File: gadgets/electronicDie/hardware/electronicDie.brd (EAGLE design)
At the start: 43.2 x 69.8 mm, 30 parts, among them IC1 CD4029N, IC2 NE555N, T1 BC327, T2 BC337, X1 USBPCB

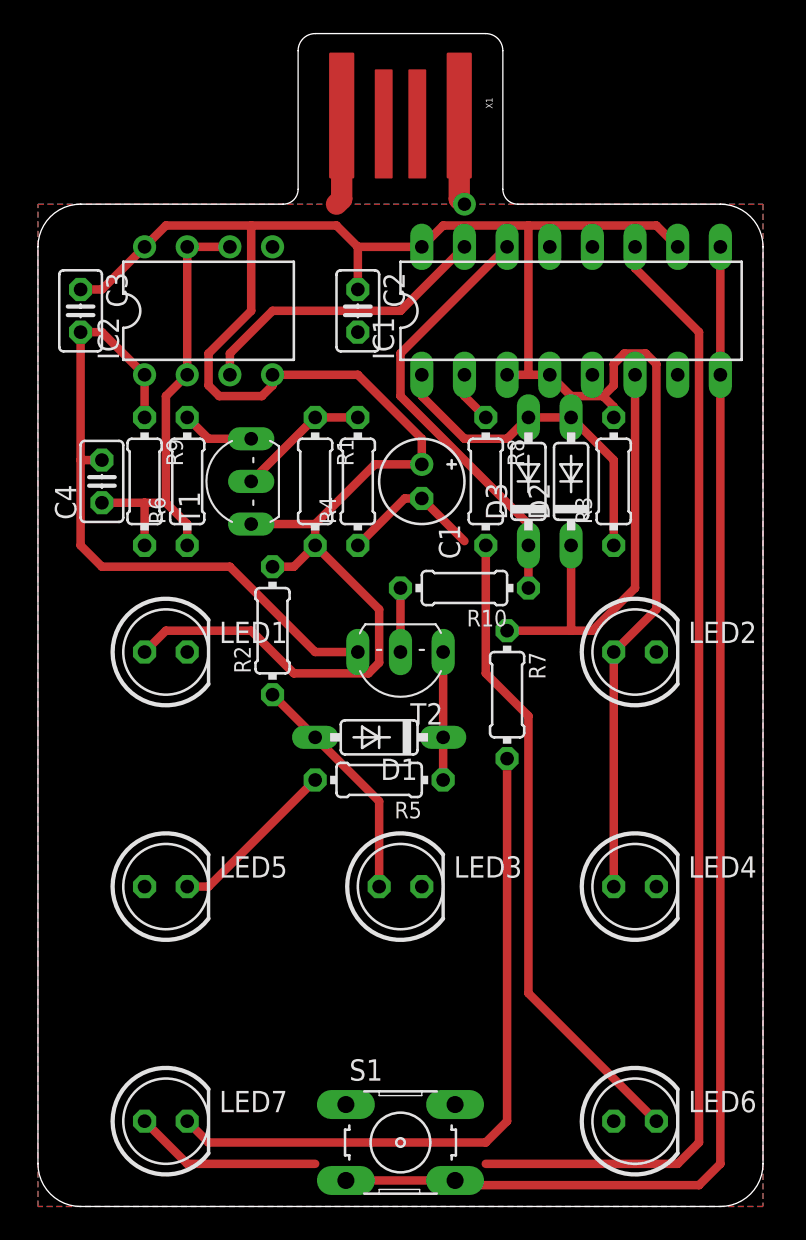
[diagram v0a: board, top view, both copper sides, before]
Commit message: Add silkscreen
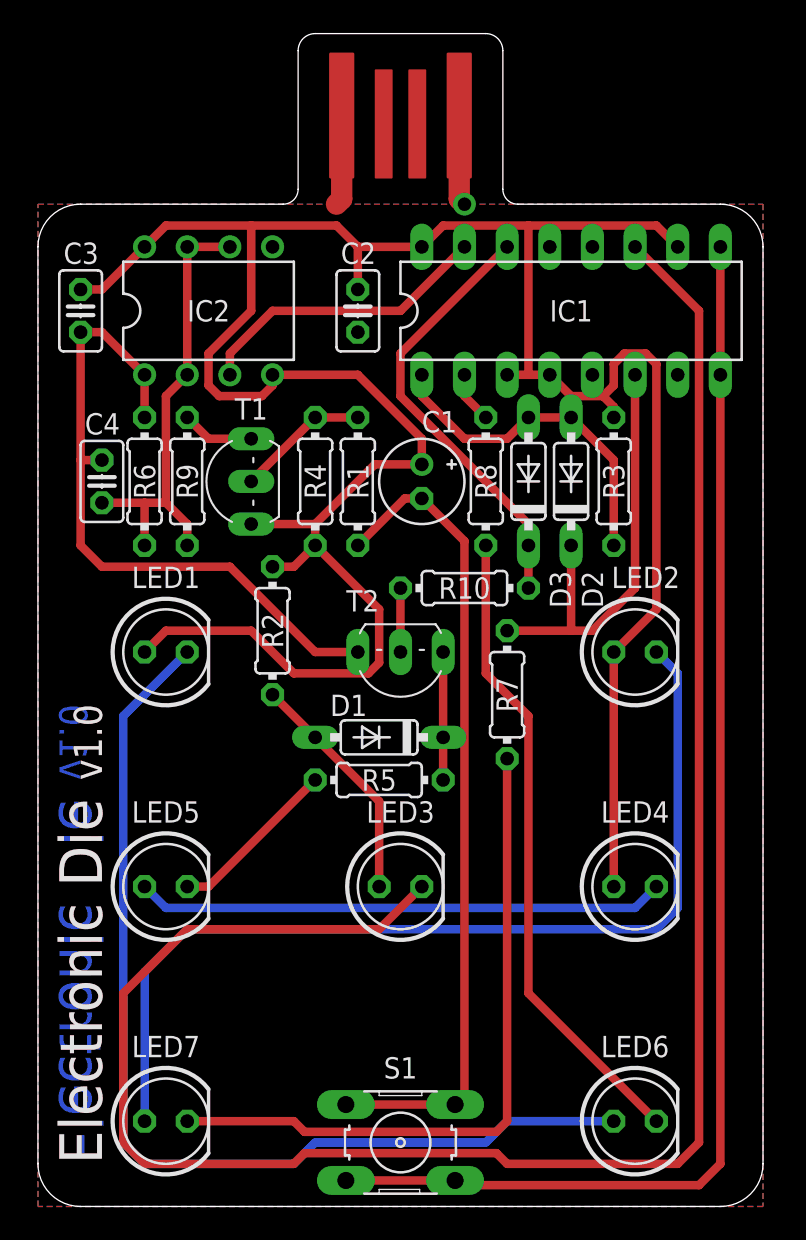
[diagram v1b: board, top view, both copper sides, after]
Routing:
- net N$16: track 0.00 -> 61.6 mm
- net N$20: track 68.1 -> 120.1 mm
- net N$14: track 11.2 -> 58.0 mm
- net N$1: track 8.56 -> 48.8 mm
- net N$13: track 0.00 -> 31.5 mm
- net N$8: track 41.7 -> 41.2 mm
- added copper zone on layer 1, net +5V
- added copper zone on layer 16, net GND
- removed copper zone on layer 1, net +5V1
- removed copper zone on layer 16, net GND1
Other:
- board text added: "+"
- board text added: "-"
- board text added: "Electronic Die"
- board text added: "RoboCamp 2021"
- board text added: "RobotikaBrno.cz Robotárna"
- board text added: "https://github.com/RoboticsBrno/RoboCamp-2021"
- board text added: "v1.0"

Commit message: Add SMD power LED for testing purposes
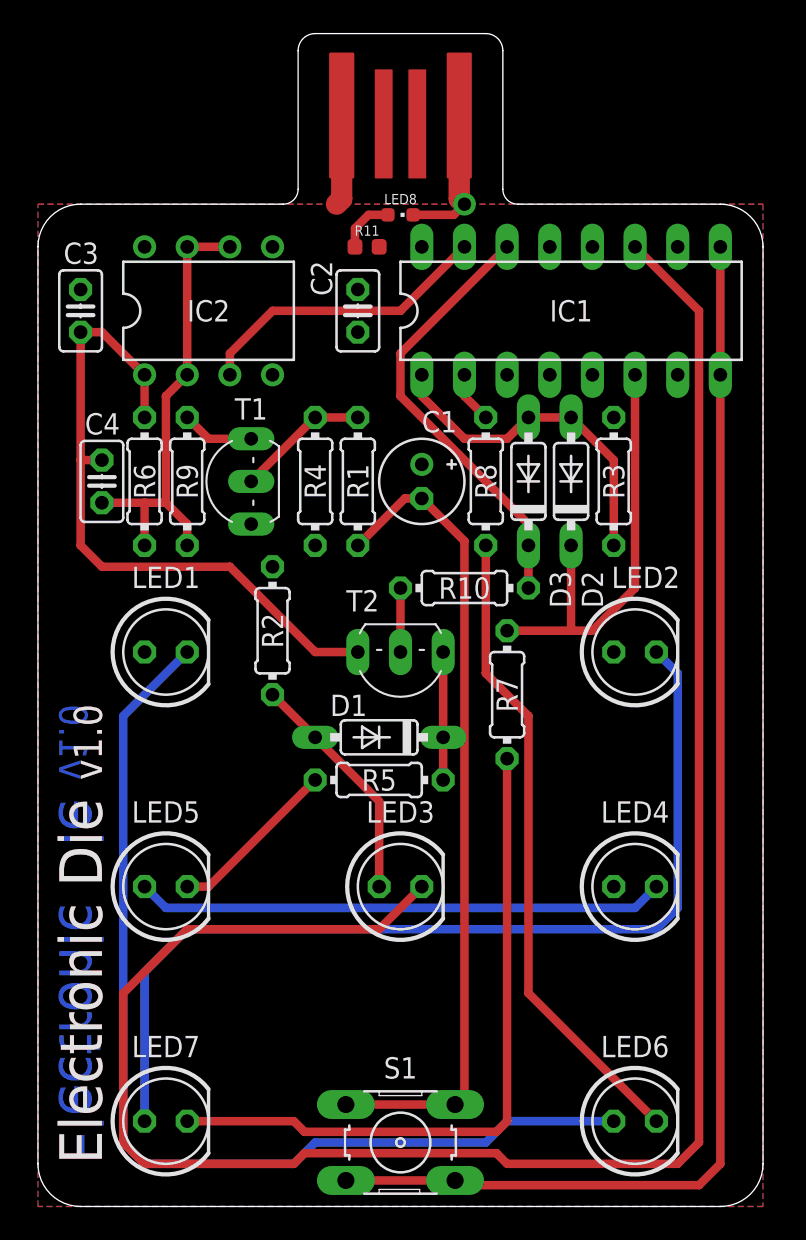
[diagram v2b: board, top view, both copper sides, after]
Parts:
- added LED8: green, led:CHIPLED_0603
- added R11: 1k, rcl_upravena:R0603
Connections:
- new net N$3: LED8.A, R11.1
- net +5V: now also R11.2
- net GND: now also LED8.C
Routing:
- net +5V: track 168.6 -> 5.41 mm
- net N$3: track 0.00 -> 3.39 mm
- net GND: track 123.5 -> 126.8 mm
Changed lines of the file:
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@@
 <layer number="21" name="tPlace" color="7" fill="1" visible="yes" active="yes"/>
 <layer number="22" name="bPlace" color="7" fill="1" visible="yes" active="yes"/>
-<layer number="23" name="tOrigins" color="15" fill="1" visible="no" active="yes"/>
+<layer number="23" name="tOrigins" color="15" fill="1" visible="yes" active="yes"/>
 <layer number="24" name="bOrigins" color="15" fill="1" visible="yes" active="yes"/>
 <layer number="25" name="tNames" color="7" fill="1" visible="yes" active="yes"/>
@@
 Robotárna</text>
 <text x="15.24" y="2.54" size="1.778" layer="102" font="vector" ratio="16" rot="SR90">RoboCamp 2021</text>
-<text x="18.415" y="59.055" size="1.27" layer="102" font="vector" ratio="16" rot="SR0">+</text>
-<text x="23.495" y="59.055" size="1.27" layer="102" font="vector" ratio="16" rot="SR0">-</text>
+<text x="16.51" y="58.42" size="1.27" layer="102" font="vector" ratio="16" rot="SR0">+</text>
+<text x="26.035" y="58.42" size="1.27" layer="102" font="vector" ratio="16" rot="SR0">-</text>
 <text x="40.64" y="2.54" size="1.27" layer="102" font="vector" ratio="16" rot="SMR90">https://github.com/RoboticsBrno/RoboCamp-2021</text>
 <text x="27.94" y="2.54" size="1.27" layer="102" font="vector" ratio="16" rot="SMR90">RobotikaBrno.cz
@@
 </element>
 <element name="C2" library="rcl_upravena" package="C025-025X050" value="100n" x="19.05" y="53.34" smashed="yes" rot="R270">
-<attribute name="NAME" x="18.034" y="56.134" size="1.27" layer="25" font="vector" ratio="16"/>
+<attribute name="NAME" x="17.526" y="54.229" size="1.27" layer="25" font="vector" ratio="16" rot="R90"/>
 <attribute name="VALUE" x="16.256" y="55.626" size="1.27" layer="27" ratio="10" rot="R270"/>
 </element>
@@
 <element name="X1" library="USB" package="USB-A-PCB" value="USBPCB" x="21.59" y="64.77" smashed="yes" rot="R270">
 <attribute name="VALUE" x="16.51" y="66.04" size="0.4064" layer="27" rot="R270"/>
+</element>
+<element name="LED8" library="led" package="CHIPLED_0603" package3d_urn="urn:adsk.eagle:package:15822/2" value="green" x="21.59" y="59.055" smashed="yes" rot="R180">
+<attribute name="NAME" x="21.59" y="59.69" size="0.6096" layer="25" font="vector" ratio="16" align="bottom-center"/>
+<attribute name="POPULARITY" value="28" x="21.59" y="59.055" size="1.27" layer="27" font="vector" ratio="16" rot="R180" display="off"/>
+<attribute name="VALUE" x="20.32" y="57.15" size="1.27" layer="27"/>
+</element>
+<element name="R11" library="rcl_upravena" package="R0603" value="1k" x="19.6" y="57.15" smashed="yes">
+<attribute name="NAME" x="19.6" y="57.8104" size="0.6096" layer="25" font="vector" ratio="16" align="bottom-center"/>
+<attribute name="VALUE" x="17.9744" y="56.6674" size="0.9906" layer="27" ratio="10"/>
 </element>
 </elements>
@@
 <vertex x="43.18" y="0"/>
 </polygon>
+<contactref element="LED8" pad="C"/>
+<wire x1="22.34" y1="59.055" x2="24.765" y2="59.055" width="0.508" layer="1"/>
+<wire x1="24.765" y1="59.055" x2="25.4" y2="59.69" width="0.508" layer="1"/>
 </signal>
 <signal name="N$2">
@@
 <wire x1="18.09" y1="64.97" x2="18.09" y2="60" width="1.27" layer="1"/>
 <wire x1="17.78" y1="59.69" x2="18.09" y2="60" width="1.27" layer="1"/>
-<wire x1="38.1" y1="57.15" x2="36.83" y2="58.42" width="0.508" layer="1"/>
-<wire x1="36.83" y1="58.42" x2="29.21" y2="58.42" width="0.508" layer="1"/>
-<wire x1="29.21" y1="58.42" x2="24.13" y2="58.42" width="0.508" layer="1"/>
-<wire x1="24.13" y1="58.42" x2="22.86" y2="57.15" width="0.508" layer="1"/>
-<wire x1="30.48" y1="49.53" x2="29.21" y2="49.53" width="0.508" layer="1"/>
-<wire x1="29.21" y1="49.53" x2="27.94" y2="49.53" width="0.508" layer="1"/>
-<wire x1="29.21" y1="49.53" x2="29.21" y2="58.42" width="0.508" layer="1"/>
-<wire x1="19.05" y1="57.15" x2="17.78" y2="58.42" width="0.508" layer="1"/>
-<wire x1="7.62" y1="58.42" x2="6.35" y2="57.15" width="0.508" layer="1"/>
-<wire x1="17.78" y1="58.42" x2="12.7" y2="58.42" width="0.508" layer="1"/>
-<wire x1="12.7" y1="58.42" x2="7.62" y2="58.42" width="0.508" layer="1"/>
-<wire x1="12.7" y1="58.42" x2="12.7" y2="53.34" width="0.508" layer="1"/>
-<wire x1="12.7" y1="53.34" x2="10.16" y2="50.8" width="0.508" layer="1"/>
-<wire x1="10.16" y1="50.8" x2="10.16" y2="48.895" width="0.508" layer="1"/>
-<wire x1="10.16" y1="48.895" x2="10.795" y2="48.26" width="0.508" layer="1"/>
-<wire x1="10.795" y1="48.26" x2="13.335" y2="48.26" width="0.508" layer="1"/>
-<wire x1="13.335" y1="48.26" x2="13.97" y2="48.895" width="0.508" layer="1"/>
-<wire x1="13.97" y1="48.895" x2="13.97" y2="49.53" width="0.508" layer="1"/>
-<wire x1="22.86" y1="44.196" x2="22.86" y2="45.72" width="0.508" layer="1"/>
-<wire x1="22.86" y1="45.72" x2="19.05" y2="49.53" width="0.508" layer="1"/>
-<wire x1="19.05" y1="49.53" x2="13.97" y2="49.53" width="0.508" layer="1"/>
-<wire x1="22.86" y1="44.196" x2="20.066" y2="44.196" width="0.508" layer="1"/>
-<wire x1="20.066" y1="44.196" x2="16.51" y2="40.64" width="0.508" layer="1"/>
-<wire x1="16.51" y1="40.64" x2="16.51" y2="39.37" width="0.508" layer="1"/>
-<wire x1="12.7" y1="40.64" x2="16.51" y2="40.64" width="0.508" layer="1"/>
-<wire x1="30.48" y1="49.53" x2="31.75" y2="48.26" width="0.508" layer="1"/>
-<wire x1="31.75" y1="48.26" x2="33.655" y2="48.26" width="0.508" layer="1"/>
-<wire x1="15.24" y1="38.1" x2="13.97" y2="38.1" width="0.508" layer="1"/>
-<wire x1="15.24" y1="38.1" x2="16.51" y2="39.37" width="0.508" layer="1"/>
-<wire x1="2.54" y1="54.61" x2="3.81" y2="54.61" width="0.508" layer="1"/>
-<wire x1="3.81" y1="54.61" x2="6.35" y2="57.15" width="0.508" layer="1"/>
-<wire x1="22.86" y1="57.15" x2="19.05" y2="57.15" width="0.508" layer="1"/>
-<wire x1="34.29" y1="19.05" x2="34.29" y2="33.02" width="0.508" layer="1"/>
-<wire x1="34.29" y1="33.02" x2="36.83" y2="35.56" width="0.508" layer="1"/>
-<wire x1="36.83" y1="35.56" x2="36.83" y2="50.165" width="0.508" layer="1"/>
-<wire x1="36.83" y1="50.165" x2="36.195" y2="50.8" width="0.508" layer="1"/>
-<wire x1="36.195" y1="50.8" x2="34.925" y2="50.8" width="0.508" layer="1"/>
-<wire x1="34.925" y1="50.8" x2="34.29" y2="50.165" width="0.508" layer="1"/>
-<wire x1="34.29" y1="50.165" x2="34.29" y2="48.895" width="0.508" layer="1"/>
-<wire x1="34.29" y1="48.895" x2="33.655" y2="48.26" width="0.508" layer="1"/>
-<wire x1="34.29" y1="46.99" x2="34.29" y2="47.625" width="0.508" layer="1"/>
-<wire x1="34.29" y1="47.625" x2="33.655" y2="48.26" width="0.508" layer="1"/>
-<wire x1="6.35" y1="33.02" x2="7.62" y2="34.29" width="0.508" layer="1"/>
-<wire x1="7.62" y1="34.29" x2="12.7" y2="34.29" width="0.508" layer="1"/>
-<wire x1="12.7" y1="34.29" x2="15.24" y2="31.75" width="0.508" layer="1"/>
-<wire x1="15.24" y1="31.75" x2="19.685" y2="31.75" width="0.508" layer="1"/>
-<wire x1="19.685" y1="31.75" x2="20.32" y2="32.385" width="0.508" layer="1"/>
-<wire x1="20.32" y1="32.385" x2="20.32" y2="35.56" width="0.508" layer="1"/>
-<wire x1="20.32" y1="35.56" x2="16.51" y2="39.37" width="0.508" layer="1"/>
-<wire x1="19.05" y1="54.61" x2="19.05" y2="57.15" width="0.508" layer="1"/>
 <polygon width="0.8128" layer="1">
 <vertex x="0" y="0"/>
@@
 <vertex x="43.18" y="0"/>
 </polygon>
+<contactref element="R11" pad="2"/>
+<wire x1="22.86" y1="44.196" x2="27.94" y2="49.53" width="0" layer="19" extent="1-1"/>
 </signal>
 <signal name="N$7">
@@
 <wire x1="36.83" y1="5.08" x2="29.21" y2="12.7" width="0.508" layer="1"/>
 </signal>
+<signal name="N$3">
+<contactref element="R11" pad="1"/>
+<contactref element="LED8" pad="A"/>
+<wire x1="20.84" y1="59.055" x2="19.685" y2="59.055" width="0.508" layer="1"/>
+<wire x1="18.88" y1="58.25" x2="18.88" y2="57.15" width="0.508" layer="1"/>
+<wire x1="19.685" y1="59.055" x2="18.88" y2="58.25" width="0.508" layer="1"/>
+</signal>
 </signals>

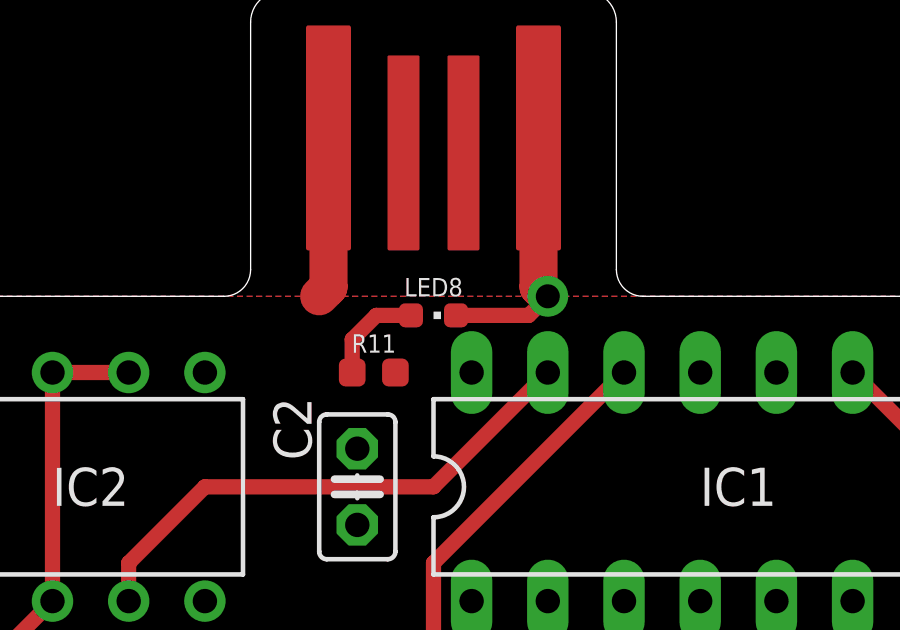
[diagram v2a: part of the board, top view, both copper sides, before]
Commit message: Fix +5V polygon
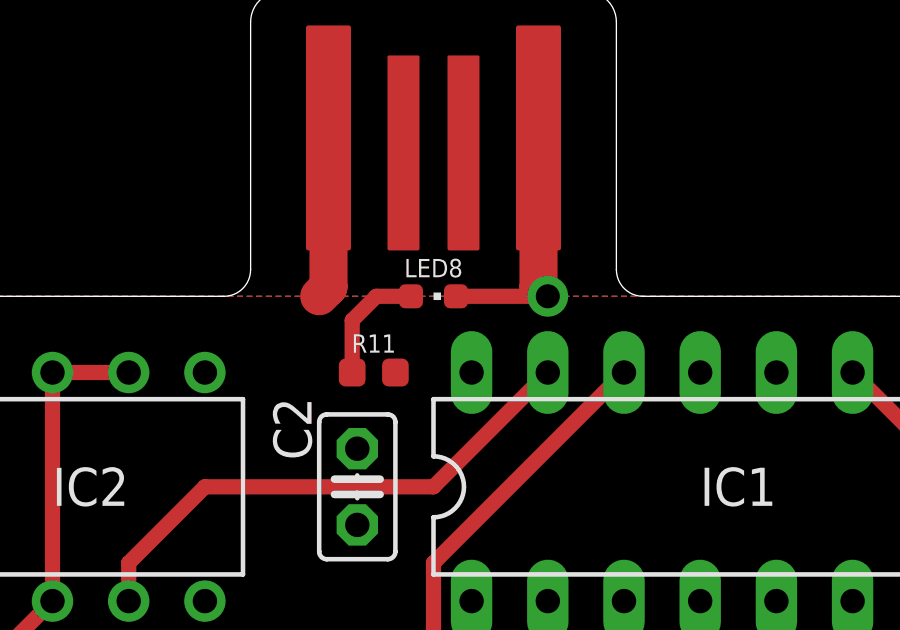
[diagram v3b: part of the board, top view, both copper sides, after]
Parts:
- moved LED8 0.63 mm to (21.6, 59.7)
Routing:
- net N$3: track 3.39 -> 4.03 mm
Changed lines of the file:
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@@
 <layer number="39" name="tKeepout" color="4" fill="11" visible="yes" active="yes"/>
 <layer number="40" name="bKeepout" color="1" fill="11" visible="yes" active="yes"/>
-<layer number="41" name="tRestrict" color="4" fill="10" visible="no" active="yes"/>
+<layer number="41" name="tRestrict" color="4" fill="10" visible="yes" active="yes"/>
 <layer number="42" name="bRestrict" color="1" fill="10" visible="no" active="yes"/>
 <layer number="43" name="vRestrict" color="2" fill="10" visible="yes" active="yes"/>
@@
 <dimension x1="0" y1="2.54" x2="43.18" y2="2.54" x3="21.59" y3="-3.81" textsize="1.27" textratio="16" layer="47"/>
 <dimension x1="2.54" y1="0" x2="17.78" y2="69.85" x3="-7.62" y3="34.925" textsize="1.27" textratio="16" layer="47" dtype="vertical"/>
+<wire x1="20.955" y1="56.7182" x2="20.955" y2="57.5818" width="0" layer="41"/>
+<wire x1="20.955" y1="57.5818" x2="20.7518" y2="57.785" width="0" layer="41"/>
+<wire x1="20.7518" y1="57.785" x2="20.0152" y2="57.785" width="0" layer="41"/>
 </plain>
 <attributes>
@@
 <attribute name="VALUE" x="16.51" y="66.04" size="0.4064" layer="27" rot="R270"/>
 </element>
-<element name="LED8" library="led" package="CHIPLED_0603" package3d_urn="urn:adsk.eagle:package:15822/2" value="green" x="21.59" y="59.055" smashed="yes" rot="R180">
-<attribute name="NAME" x="21.59" y="59.69" size="0.6096" layer="25" font="vector" ratio="16" align="bottom-center"/>
-<attribute name="POPULARITY" value="28" x="21.59" y="59.055" size="1.27" layer="27" font="vector" ratio="16" rot="R180" display="off"/>
-<attribute name="VALUE" x="20.32" y="57.15" size="1.27" layer="27"/>
+<element name="LED8" library="led" package="CHIPLED_0603" package3d_urn="urn:adsk.eagle:package:15822/2" value="green" x="21.59" y="59.69" smashed="yes" rot="R180">
+<attribute name="NAME" x="21.59" y="60.325" size="0.6096" layer="25" font="vector" ratio="16" align="bottom-center"/>
+<attribute name="POPULARITY" value="28" x="21.59" y="59.69" size="1.27" layer="27" font="vector" ratio="16" rot="R180" display="off"/>
+<attribute name="VALUE" x="20.32" y="57.785" size="1.27" layer="27"/>
 </element>
 <element name="R11" library="rcl_upravena" package="R0603" value="1k" x="19.6" y="57.15" smashed="yes">
@@
 <wire x1="39.37" y1="1.27" x2="40.64" y2="2.54" width="0.508" layer="1"/>
 <wire x1="40.64" y1="2.54" x2="40.64" y2="49.53" width="0.508" layer="1"/>
-<polygon width="0.8128" layer="16">
+<polygon width="0.6096" layer="16">
 <vertex x="0" y="0"/>
 <vertex x="0" y="59.69"/>
@@
 </polygon>
 <contactref element="LED8" pad="C"/>
-<wire x1="22.34" y1="59.055" x2="24.765" y2="59.055" width="0.508" layer="1"/>
-<wire x1="24.765" y1="59.055" x2="25.4" y2="59.69" width="0.508" layer="1"/>
+<wire x1="25.4" y1="59.69" x2="22.34" y2="59.69" width="0.508" layer="1"/>
 </signal>
 <signal name="N$2">
@@
 <wire x1="18.09" y1="64.97" x2="18.09" y2="60" width="1.27" layer="1"/>
 <wire x1="17.78" y1="59.69" x2="18.09" y2="60" width="1.27" layer="1"/>
-<polygon width="0.8128" layer="1">
+<polygon width="0.6096" layer="1">
 <vertex x="0" y="0"/>
 <vertex x="0" y="59.69"/>
@@
 </polygon>
 <contactref element="R11" pad="2"/>
-<wire x1="22.86" y1="44.196" x2="27.94" y2="49.53" width="0" layer="19" extent="1-1"/>
 </signal>
 <signal name="N$7">
@@
 <contactref element="R11" pad="1"/>
 <contactref element="LED8" pad="A"/>
-<wire x1="20.84" y1="59.055" x2="19.685" y2="59.055" width="0.508" layer="1"/>
-<wire x1="18.88" y1="58.25" x2="18.88" y2="57.15" width="0.508" layer="1"/>
-<wire x1="19.685" y1="59.055" x2="18.88" y2="58.25" width="0.508" layer="1"/>
+<wire x1="20.84" y1="59.69" x2="19.685" y2="59.69" width="0.508" layer="1"/>
+<wire x1="18.88" y1="58.885" x2="18.88" y2="57.15" width="0.508" layer="1"/>
+<wire x1="19.685" y1="59.69" x2="18.88" y2="58.885" width="0.508" layer="1"/>
 </signal>
 </signals>
